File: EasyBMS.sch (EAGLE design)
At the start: 166 parts, among them IC1 LM2596S-5.0_NOPB, IC2 LTC6811IG-1#PBF, Q10 BSS84LT1G, Q11 BSS84LT1G, Q12 BSS84LT1G, Q13 BSS84LT1G, Q2 BSS84LT1G, Q3 BSS84LT1G, Q4 BSS84LT1G, Q5 BSS84LT1G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

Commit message: bug on 2 LEDs removed, new production files generated
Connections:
- removed net N$3: LED1.C, LED2.C
- net GND: now also LED1.C, LED2.C
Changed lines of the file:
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@@
 <setting verticaltext="up"/>
 </settings>
-<grid distance="0.1" unitdist="inch" unit="inch" style="lines" multiple="1" display="no" altdistance="0.01" altunitdist="inch" altunit="inch"/>
+<grid distance="0.01" unitdist="inch" unit="inch" style="dots" multiple="1" display="yes" altdistance="0.01" altunitdist="inch" altunit="inch"/>
 <layers>
 <layer number="1" name="Top" color="4" fill="1" visible="no" active="no"/>
@@
 <wire x1="78.105" y1="315.595" x2="78.105" y2="307.975" width="0.1524" layer="91"/>
 <label x="75.565" y="305.435" size="1.778" layer="95"/>
+<pinref part="LED2" gate="G$1" pin="C"/>
+<pinref part="LED1" gate="G$1" pin="C"/>
+<wire x1="74.93" y1="346.075" x2="78.105" y2="346.075" width="0.1524" layer="91"/>
+<wire x1="78.105" y1="346.075" x2="78.105" y2="335.915" width="0.1524" layer="91"/>
+<wire x1="78.105" y1="335.915" x2="74.93" y2="335.915" width="0.1524" layer="91"/>
+<wire x1="74.93" y1="315.595" x2="74.93" y2="335.915" width="0.1524" layer="91"/>
+<junction x="74.93" y="315.595"/>
+<junction x="74.93" y="335.915"/>
 </segment>
 <segment>
@@
 </segment>
 </net>
-<net name="N$3" class="0">
-<segment>
-<pinref part="LED2" gate="G$1" pin="C"/>
-<pinref part="LED1" gate="G$1" pin="C"/>
-<wire x1="74.93" y1="346.075" x2="78.105" y2="346.075" width="0.1524" layer="91"/>
-<wire x1="78.105" y1="346.075" x2="78.105" y2="335.915" width="0.1524" layer="91"/>
-<wire x1="78.105" y1="335.915" x2="74.93" y2="335.915" width="0.1524" layer="91"/>
-</segment>
-</net>

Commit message: level shifter removed
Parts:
- removed R100, R101, R102, R103, R55, R59, R60, R82, R96, R97, R98, R99: 10k, rcl:R-EU_R0603
- removed T1, T2, T3, T4, T5, T6: C8545, zetex:NMOSSOT23
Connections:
- removed net A0DC: JP1.4, R101.1, T5.D
- removed net CSB: IC2.CSB_(IMA), R99.1, T4.D
- removed net CSDSPLESP: R102.1, T6.S, U$2.D0
- removed net CSLTCESP: R98.1, T4.S, U$2.D8
- removed net MISOESP: R60.1, T2.S, U$2.D6
- removed net MOSIESP: R96.1, T3.S, U$2.D7
- removed net SCKESP: R55.1, T1.S, U$2.D5
- new net CSLTC: IC2.CSB_(IMA), U$2.D8
- net +3V3: now also JP1.1; no longer R100.2, R102.2, R55.2, R60.2, R96.2, R98.2, T1.G, T2.G, T3.G, T4.G, T5.G, T6.G
- net 5VINESP: no longer JP1.1, R101.2, R103.2, R59.2, R82.2, R97.2, R99.2
- net CSDSPL: now also U$2.D0; no longer R103.1, T6.D
- net D3: now also JP1.4; no longer R100.1, T5.S
- net MISO: now also U$2.D6; no longer R82.1, T2.D
- net MOSI: now also U$2.D7; no longer R97.1, T3.D
- net SCK: now also U$2.D5; no longer R59.1, T1.D
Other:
- note removed: "3,3"
- note removed: "5"

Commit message: design blocks added
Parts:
- added R2: 10k, rcl:R-EU_R1206
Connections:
- net +3V3: now also R2.2
- net MISO: now also R2.1
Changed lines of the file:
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@@
 <setting verticaltext="up"/>
 </settings>
-<grid distance="0.1" unitdist="inch" unit="inch" style="lines" multiple="1" display="no" altdistance="0.01" altunitdist="inch" altunit="inch"/>
+<grid distance="0.025" unitdist="inch" unit="inch" style="lines" multiple="1" display="yes" altdistance="0.01" altunitdist="inch" altunit="inch"/>
 <layers>
 <layer number="1" name="Top" color="4" fill="1" visible="no" active="no"/>
@@
 <part name="GND1" library="supply1" library_urn="urn:adsk.eagle:library:371" deviceset="GND" device=""/>
 <part name="JP1" library="pinhead" library_urn="urn:adsk.eagle:library:325" deviceset="PINHD-1X8" device="" package3d_urn="urn:adsk.eagle:package:22409/2"/>
+<part name="R2" library="rcl" library_urn="urn:adsk.eagle:library:334" deviceset="R-EU_" device="R1206" package3d_urn="urn:adsk.eagle:package:23540/2" value="10k"/>
+<part name="+3V1" library="supply1" library_urn="urn:adsk.eagle:library:371" deviceset="+3V3" device=""/>
 </parts>
 <sheets>
@@
 <attribute name="VALUE" x="180.975" y="351.79" size="1.778" layer="96"/>
 </instance>
+<instance part="R2" gate="G$1" x="-60.96" y="323.215" smashed="yes" rot="R90">
+<attribute name="NAME" x="-62.4586" y="319.405" size="1.778" layer="95" rot="R90"/>
+<attribute name="VALUE" x="-57.658" y="319.405" size="1.778" layer="96" rot="R90"/>
+</instance>
+<instance part="+3V1" gate="G$1" x="-62.23" y="338.455" smashed="yes">
+<attribute name="VALUE" x="-64.77" y="333.375" size="1.778" layer="96" rot="R90"/>
+</instance>
 </instances>
 <busses>
@@
 <segment>
 <pinref part="U$2" gate="G$1" pin="D6"/>
-<wire x1="-6.35" y1="313.055" x2="-16.51" y2="313.055" width="0.1524" layer="91"/>
 <label x="-27.94" y="312.42" size="1.778" layer="95"/>
+<wire x1="-6.35" y1="313.055" x2="-60.96" y2="313.055" width="0.1524" layer="91"/>
+<pinref part="R2" gate="G$1" pin="1"/>
+<wire x1="-60.96" y1="318.135" x2="-60.96" y2="313.055" width="0.1524" layer="91"/>
 </segment>
 </net>
@@
 <label x="170.815" y="375.285" size="1.778" layer="95"/>
 </segment>
-</net>
+<segment>
+<pinref part="R2" gate="G$1" pin="2"/>
+<wire x1="-60.96" y1="328.295" x2="-60.96" y2="332.74" width="0.1524" layer="91"/>
+<pinref part="+3V1" gate="G$1" pin="+3V3"/>
+<wire x1="-62.23" y1="335.915" x2="-62.23" y2="332.74" width="0.1524" layer="91"/>
+<wire x1="-62.23" y1="332.74" x2="-60.96" y2="332.74" width="0.1524" layer="91"/>
+</segment>
+</net>

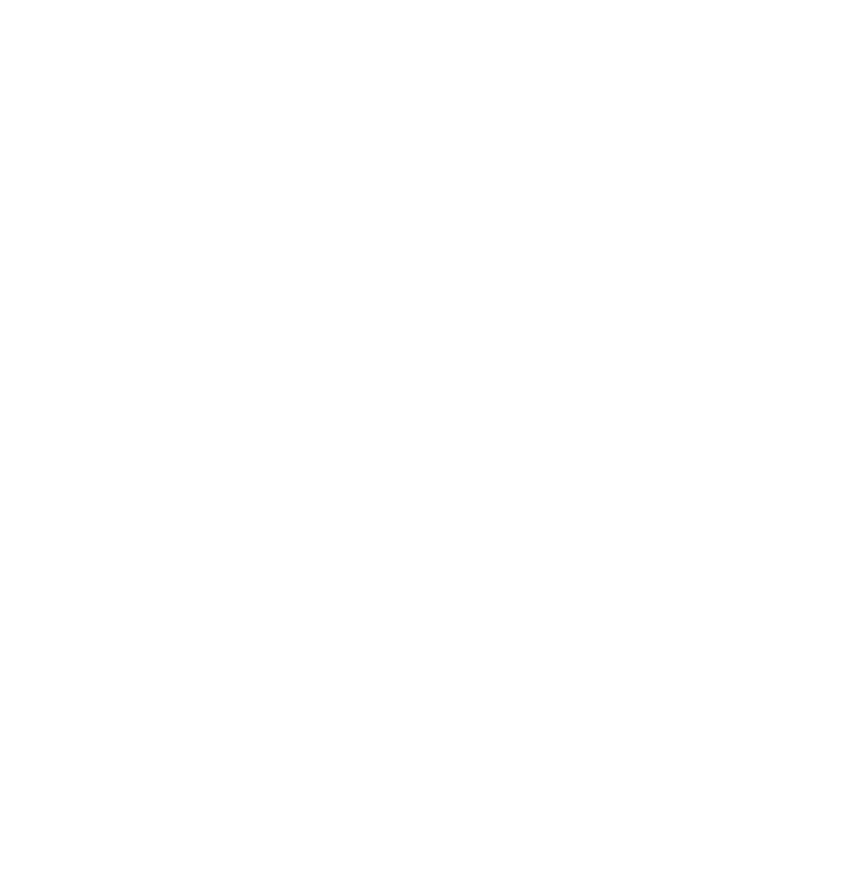
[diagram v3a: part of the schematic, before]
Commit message: New controller added as part
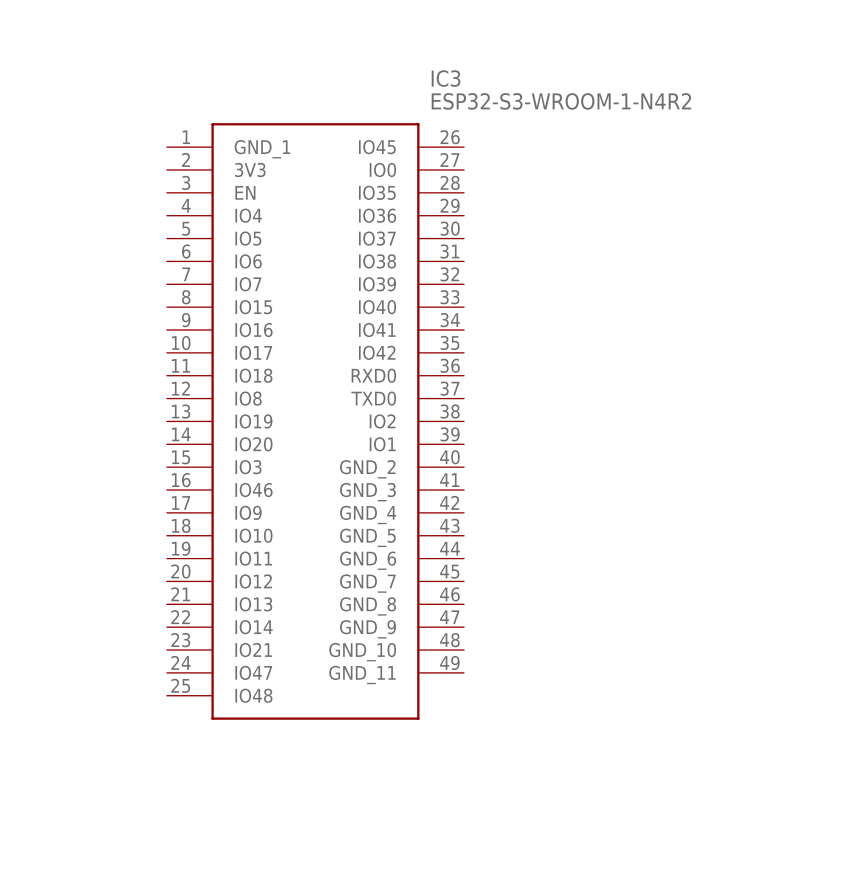
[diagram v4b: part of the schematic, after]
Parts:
- added IC3: ESP32-S3-WROOM-1-N4R2, SamacSys_Parts:ESP32-S3-WROOM-1-N4R2
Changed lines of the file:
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@@
 <setting verticaltext="up"/>
 </settings>
-<grid distance="0.025" unitdist="inch" unit="inch" style="lines" multiple="1" display="yes" altdistance="0.01" altunitdist="inch" altunit="inch"/>
+<grid distance="0.1" unitdist="inch" unit="inch" style="lines" multiple="1" display="no" altdistance="0.01" altunitdist="inch" altunit="inch"/>
 <layers>
 <layer number="1" name="Top" color="4" fill="1" visible="no" active="no"/>
@@
 <part name="R2" library="rcl" library_urn="urn:adsk.eagle:library:334" deviceset="R-EU_" device="R1206" package3d_urn="urn:adsk.eagle:package:23540/2" value="10k"/>
 <part name="+3V1" library="supply1" library_urn="urn:adsk.eagle:library:371" deviceset="+3V3" device=""/>
+<part name="IC3" library="SamacSys_Parts" deviceset="ESP32-S3-WROOM-1-N4R2" device=""/>
 </parts>
 <sheets>
@@
 <attribute name="VALUE" x="-64.77" y="333.375" size="1.778" layer="96" rot="R90"/>
 </instance>
+<instance part="IC3" gate="G$1" x="132.08" y="627.38" smashed="yes">
+<attribute name="NAME" x="161.29" y="635" size="1.778" layer="95" align="center-left"/>
+<attribute name="VALUE" x="161.29" y="632.46" size="1.778" layer="96" align="center-left"/>
+</instance>
 </instances>

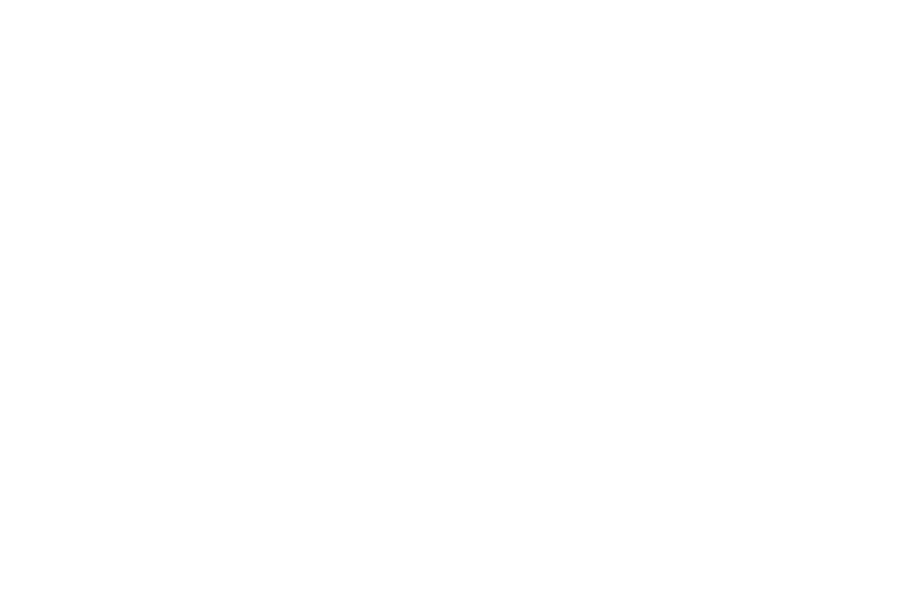
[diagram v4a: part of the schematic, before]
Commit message: dummy IC added
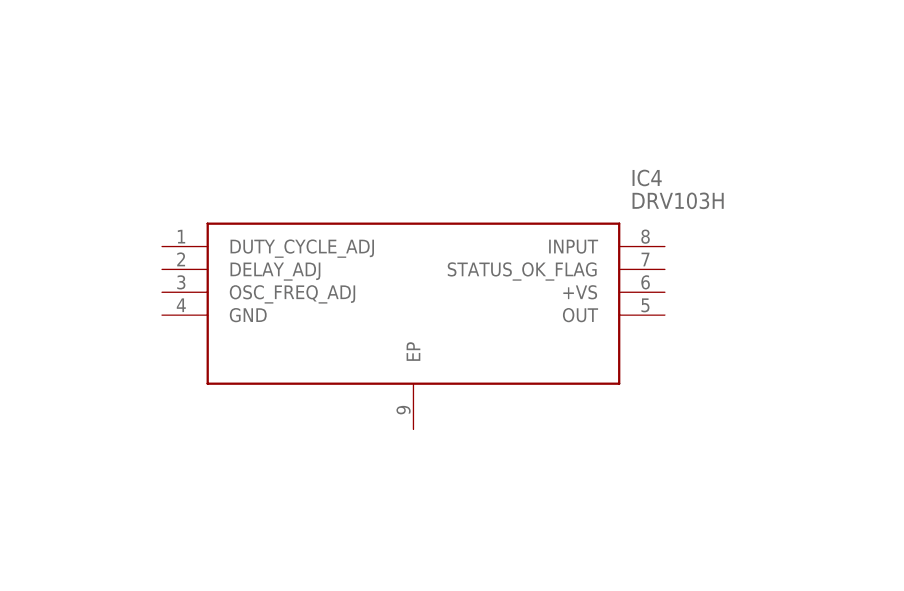
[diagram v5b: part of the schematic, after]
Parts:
- added IC4: DRV103H, SamacSys_Parts:DRV103H
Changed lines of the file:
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@@
 <part name="+3V1" library="supply1" library_urn="urn:adsk.eagle:library:371" deviceset="+3V3" device=""/>
 <part name="IC3" library="SamacSys_Parts" deviceset="ESP32-S3-WROOM-1-N4R2" device=""/>
+<part name="IC4" library="SamacSys_Parts" deviceset="DRV103H" device=""/>
 </parts>
 <sheets>
@@
 <attribute name="VALUE" x="161.29" y="632.46" size="1.778" layer="96" align="center-left"/>
 </instance>
+<instance part="IC4" gate="G$1" x="-38.1" y="596.9" smashed="yes">
+<attribute name="NAME" x="13.97" y="604.52" size="1.778" layer="95" align="center-left"/>
+<attribute name="VALUE" x="13.97" y="601.98" size="1.778" layer="96" align="center-left"/>
+</instance>
 </instances>
